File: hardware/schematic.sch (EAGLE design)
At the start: 23 parts, among them X1 SMA-142-0701-801/806

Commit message: added a bit of more parts to op-amp (trying to reduce the noise)
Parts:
- added C5: 10pF, capacitor-wima:C2.5/2
- added R8: 100, resistor:R-US_0204/2V
- added R9: 100K, resistor:R-US_0204/2V
- C3: value 1nF -> 100pF
- R3: value 47K -> 470K
- R4: value 100K -> 1M
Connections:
- removed net N$4: C3.1, LMC6482.1, LMC6482.2
- new net N$11: HX1_B.1, R7.1
- new net N$12: C5.2, LMC6482.2, R9.1
- new net N$13: C5.1, LMC6482.1, R8.1, R9.2
- net +5V: now also HX1_B.2; no longer HX1_B.1
- net N$8: now also C3.1, R8.2; no longer HX1_B.2, R7.1
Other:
- note added: "PIN 1 IS ENABLE AND WE NEED TO FIGURE OUT HOW ARE WE GOING TO WIRE IT TO GPIO"
- note removed: "PIN 3 IS ENABLE AND WE NEED TO FIGURE OUT HOW ARE WE GOING TO WIRE IT TO GPIO"
- moved on the sheet: C3, R3, R4, R7

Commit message: added schematics to disable unused op-amp
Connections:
- new net N$4: LMC6482.6, LMC6482.7
- net GNDA: now also LMC6482.5
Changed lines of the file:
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@@
 <part name="R9" library="resistor" deviceset="R-US_" device="0204/2V" value="100K"/>
 <part name="C5" library="capacitor-wima" deviceset="C" device="2.5/2" value="10pF"/>
+<part name="GND9" library="supply1" deviceset="GNDA" device=""/>
 </parts>
 <sheets>
@@
 <instance part="R9" gate="G$1" x="48.26" y="25.4" rot="R90"/>
 <instance part="C5" gate="G$1" x="58.42" y="25.4"/>
+<instance part="GND9" gate="1" x="88.9" y="0"/>
 </instances>
 <busses>
@@
 <pinref part="TIVA_PWR" gate="A" pin="3"/>
 <wire x1="-35.56" y1="25.4" x2="-22.86" y2="25.4" width="0.1524" layer="91"/>
+</segment>
+<segment>
+<pinref part="LMC6482" gate="G$1" pin="5"/>
+<wire x1="86.36" y1="10.16" x2="88.9" y2="10.16" width="0.1524" layer="91"/>
+<pinref part="GND9" gate="1" pin="GNDA"/>
+<wire x1="88.9" y1="10.16" x2="88.9" y2="2.54" width="0.1524" layer="91"/>
 </segment>
 </net>
@@
 </segment>
 </net>
+<net name="N$4" class="0">
+<segment>
+<pinref part="LMC6482" gate="G$1" pin="7"/>
+<wire x1="86.36" y1="15.24" x2="88.9" y2="15.24" width="0.1524" layer="91"/>
+<wire x1="88.9" y1="15.24" x2="88.9" y2="12.7" width="0.1524" layer="91"/>
+<pinref part="LMC6482" gate="G$1" pin="6"/>
+<wire x1="88.9" y1="12.7" x2="86.36" y2="12.7" width="0.1524" layer="91"/>
+</segment>
+</net>

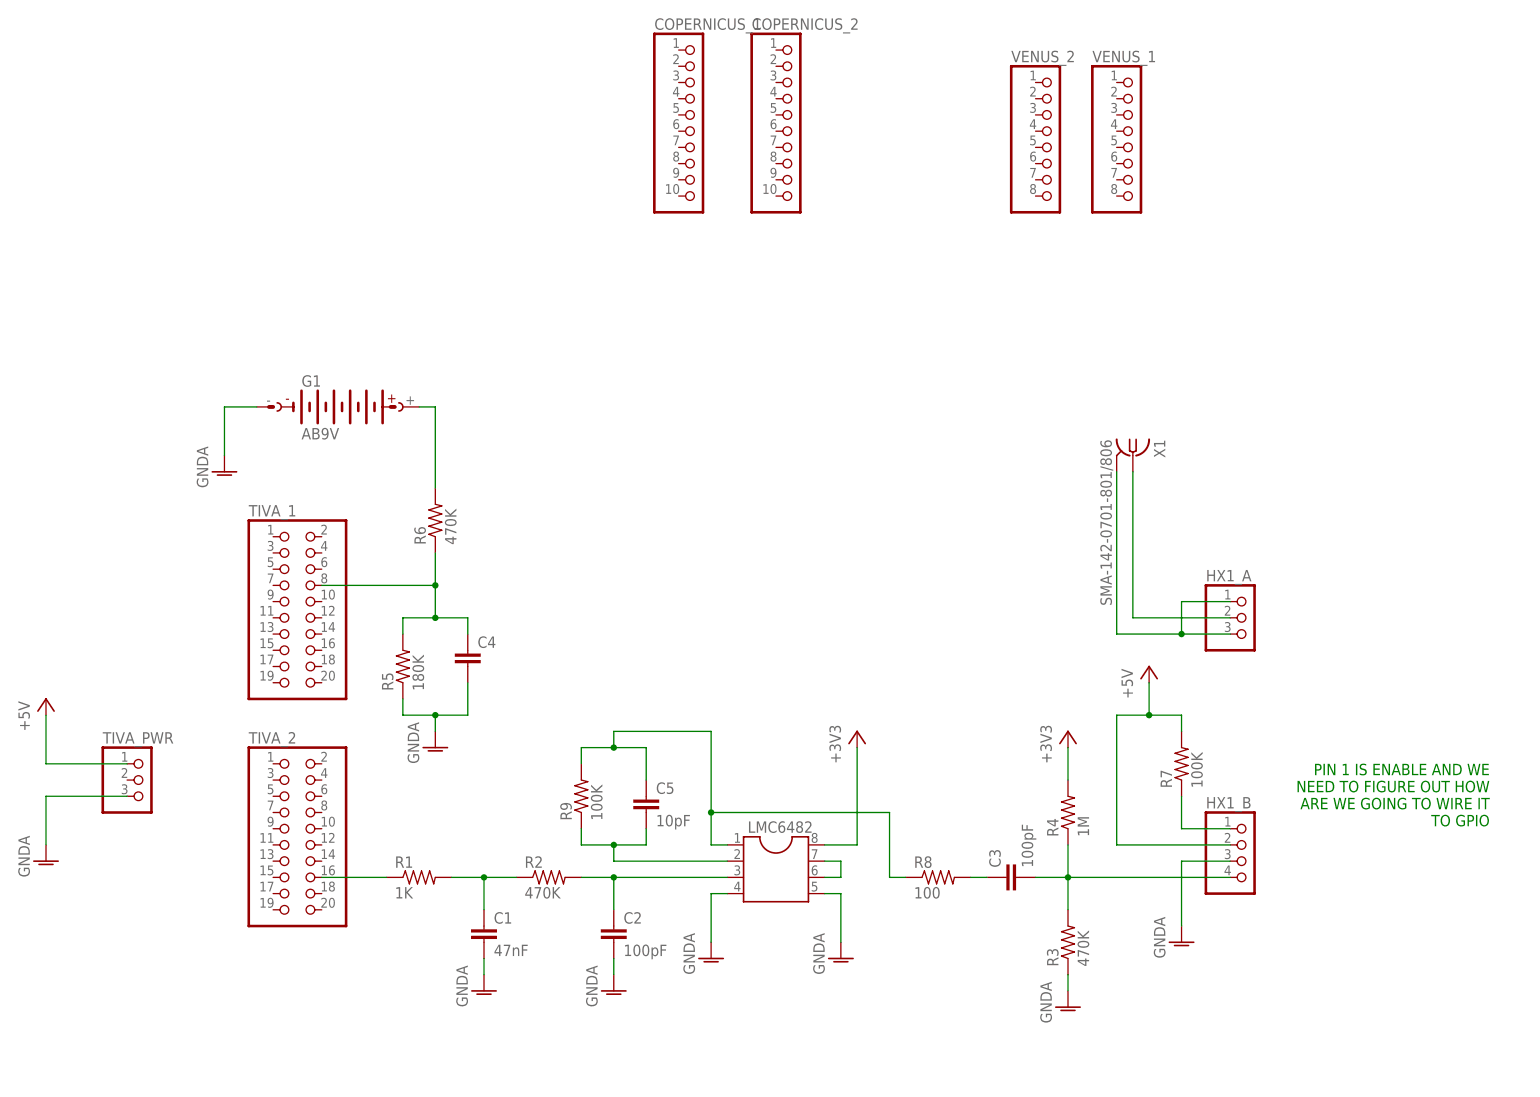
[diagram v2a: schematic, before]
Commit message: fixed R9 wiring, added capacitor for power
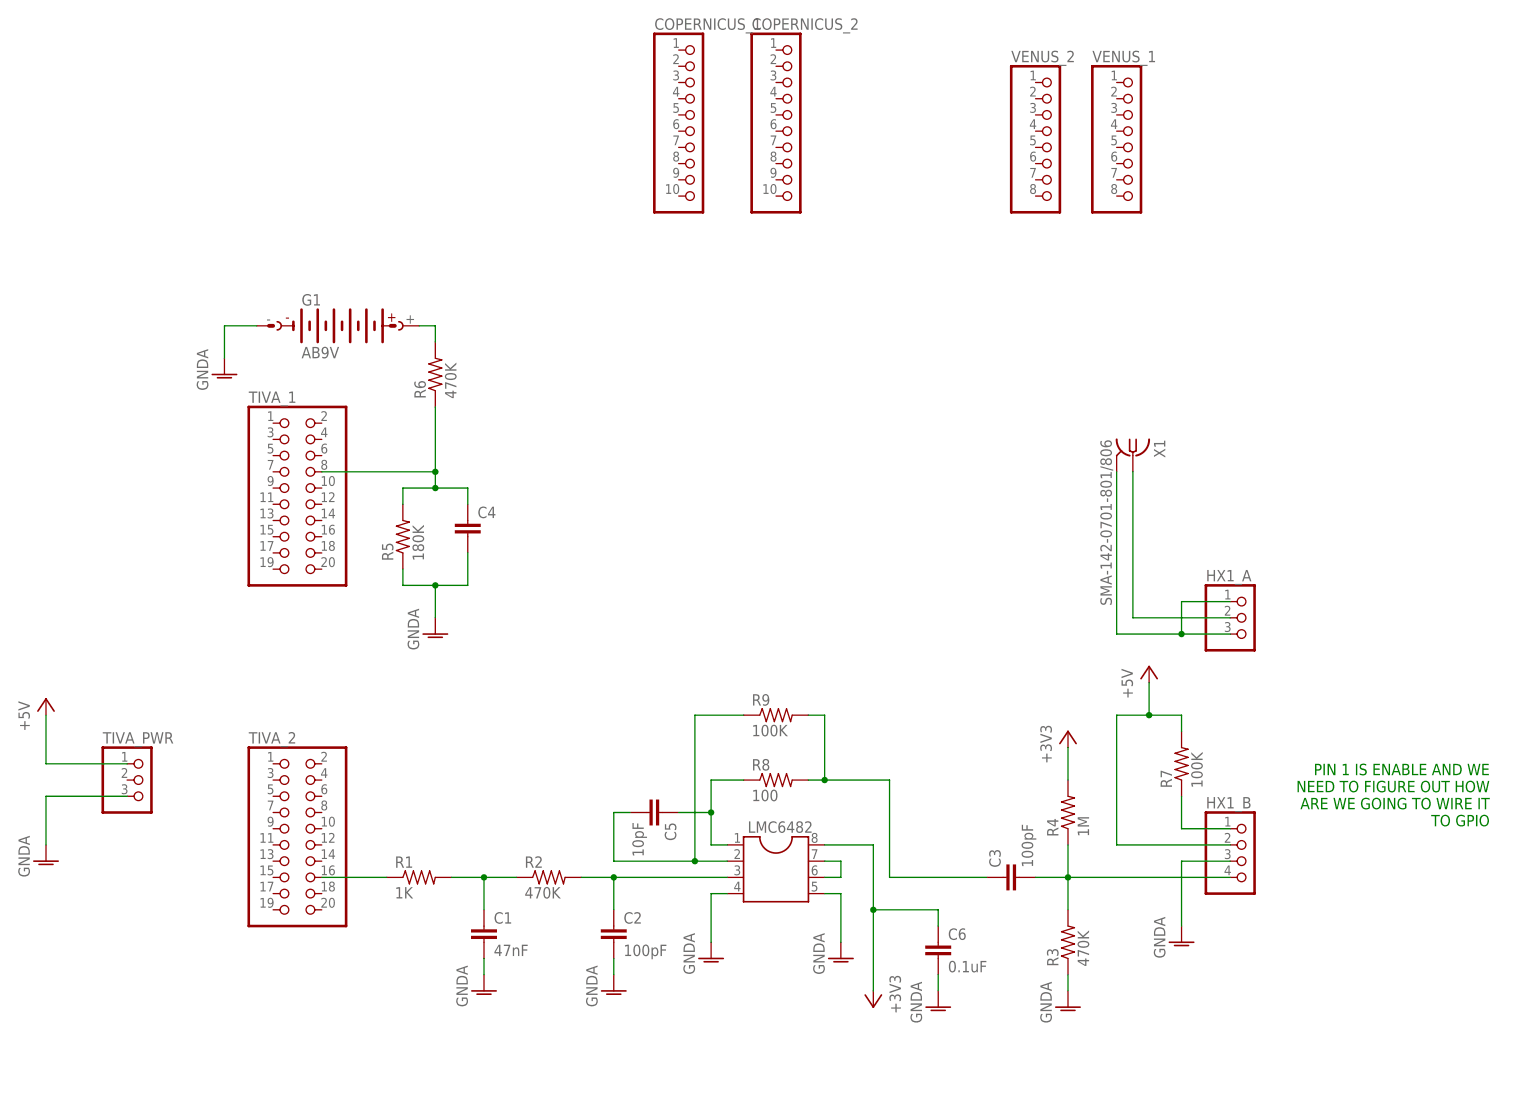
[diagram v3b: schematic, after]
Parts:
- added C6: 0.1uF, capacitor-wima:C2.5/2
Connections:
- net +3V3: now also C6.1
- net GNDA: now also C6.2
- net N$13: no longer R9.2
- net N$8: now also R9.2
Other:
- moved on the sheet: C4, C5, G1, R5, R6, R8, R9, TIVA_1

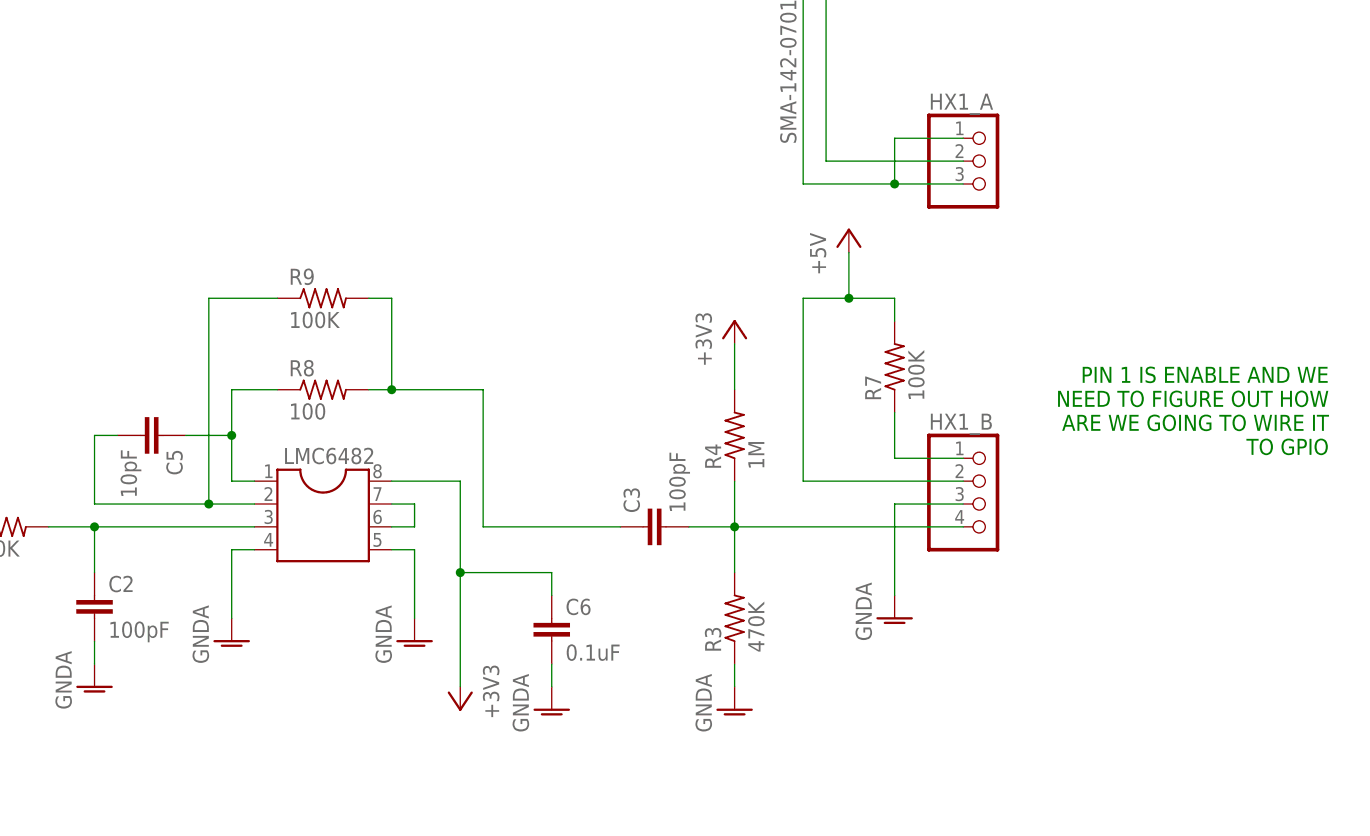
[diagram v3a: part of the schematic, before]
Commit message: now utilizing opamp to separate high pass filter from hx1
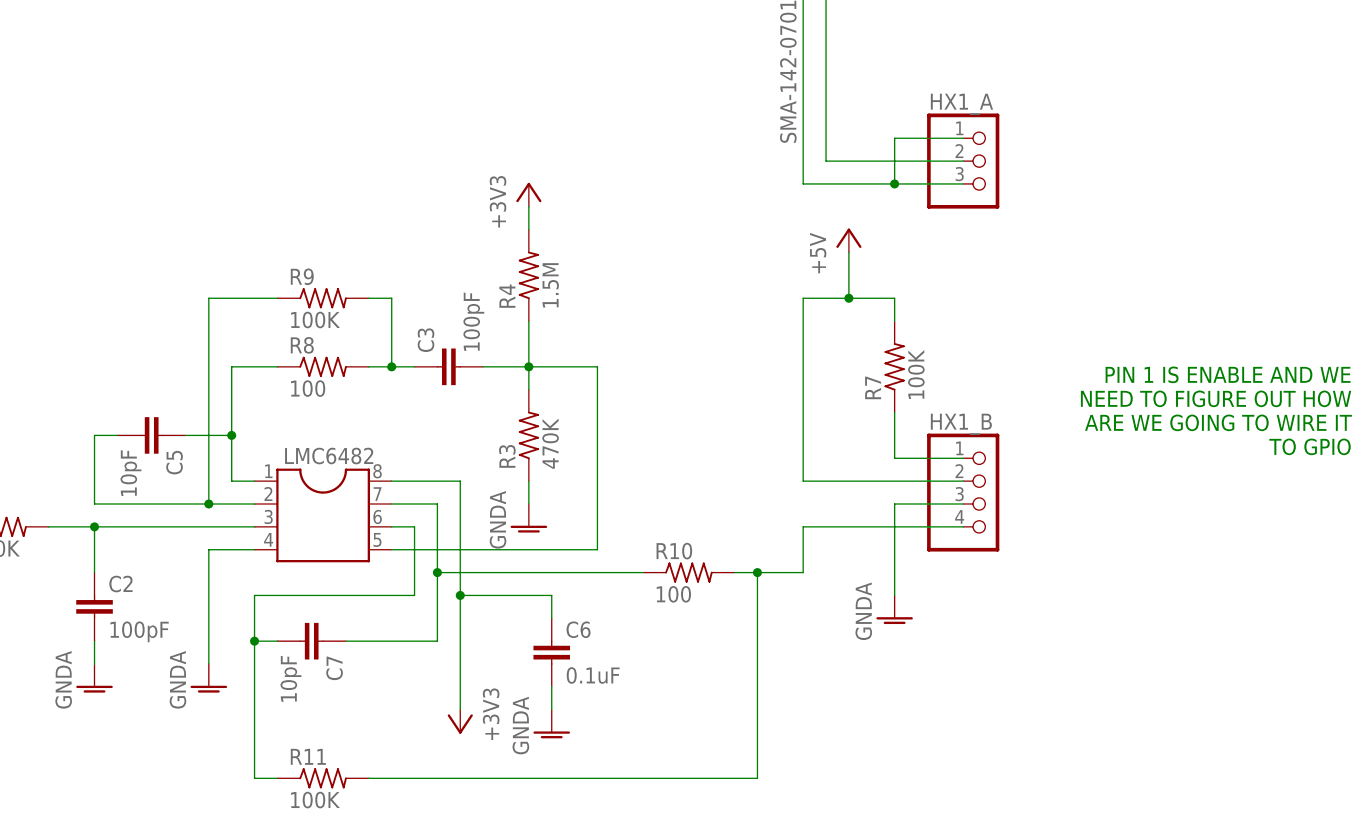
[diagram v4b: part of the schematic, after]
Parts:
- added C7: 10pF, capacitor-wima:C2.5/2
- added R10: 100, resistor:R-US_0204/2V
- added R11: 100K, resistor:R-US_0204/2V
- R4: value 1M -> 1.5M
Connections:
- new net N$12: C7.1, LMC6482.7, R10.1
- new net N$14: HX1_B.4, R10.2, R11.2
- net GNDA: no longer LMC6482.5
- net N$4: now also C7.2, R11.1; no longer LMC6482.7
- net N$6: now also LMC6482.5; no longer HX1_B.4
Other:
- moved on the sheet: C3, C6, R3, R4, R8
